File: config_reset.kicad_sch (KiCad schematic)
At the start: 23 parts, among them U1 NX1H35 PBGA625, U6 M95P32-IXMNT/E, Y2 LFSPXO025225_25MHz

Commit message: pre-order adjustments
DF9 connectors footprint adjusted.
Dimensions of board edges changed.
Placement of DF9 adjusted.
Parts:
- removed R7: 10k, Resistor_SMD:R_0402_1005Metric_Pad0.72x0.64mm_HandSolder, symbol Device:R_Small
- renumbered C14 to C13, C110 to C14, D6 to D1, D7 to D2, D5 to D3, D3 to D5, D1 to D6, R27 to R1, R3 to R10, R1 to R11, R31 to R2, R33 to R3, R32 to R4, R19 to R5, R9 to R6, R14 to R7, R6 to R8, R8 to R9, U6 to U2, Y2 to Y1
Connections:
- no-connect marks 86 -> 87

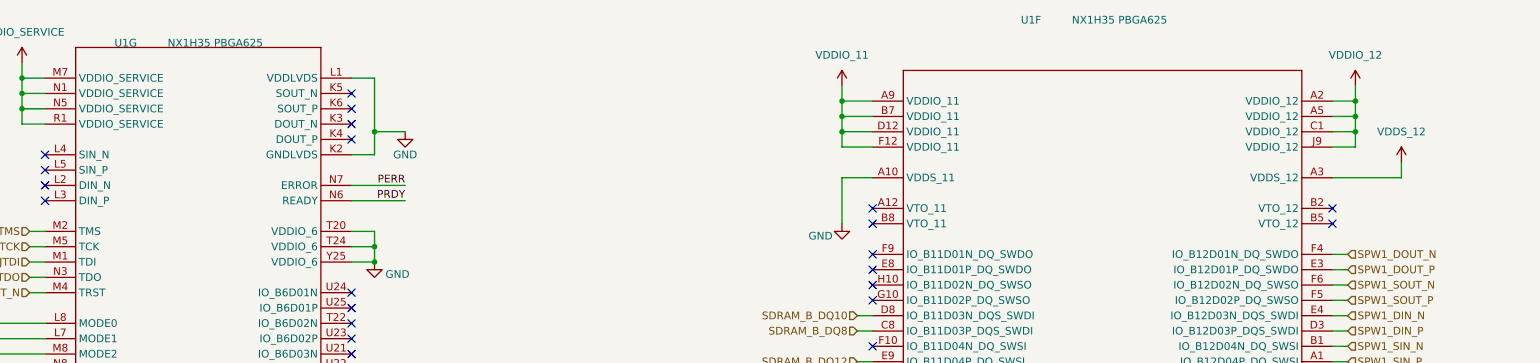
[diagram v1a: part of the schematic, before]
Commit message: pre order adjustments. Board symmetry
adjusted little things brought up by DFM checker of JLCPCB. Board's edges fully symmetrical on y axis. 2mm shift on x axis of the DF9s maintained
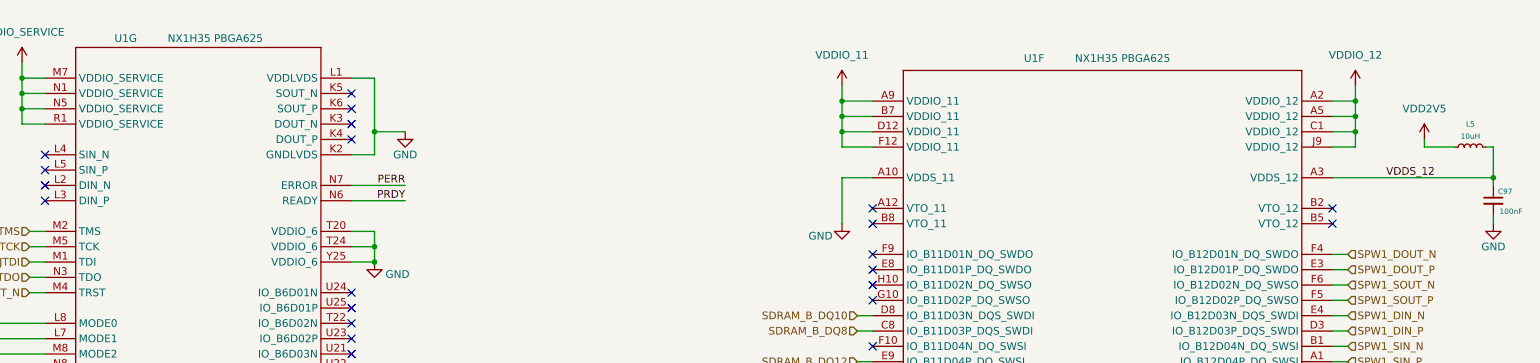
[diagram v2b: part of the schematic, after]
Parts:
- added C97: 100nF, Capacitor_SMD:C_0402_1005Metric_Pad0.74x0.62mm_HandSolder, symbol Device:C_Small
- added L5: 10uH, Inductor_SMD:L_0603_1608Metric_Pad1.05x0.95mm_HandSolder, symbol Device:L_Small
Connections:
- net GND: now also C97.2
- net VDD2V5: now also L5.2
- net VDDS_12: now also C97.1, L5.1
